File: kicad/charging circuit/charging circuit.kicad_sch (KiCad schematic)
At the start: 21 parts, among them J10 Amphenol PL00Y-301-10M8, J12 Amphenol PL00X-301-10M8, J16 Amphenol PL00X-301-10M8, J17 Amphenol PL00Y-301-10M8, J2 Conn_01x06, J3 Conn_01x08, J34 amphenolpl00Y, J35 Conn_01x03, SW20 SW_Push_Open

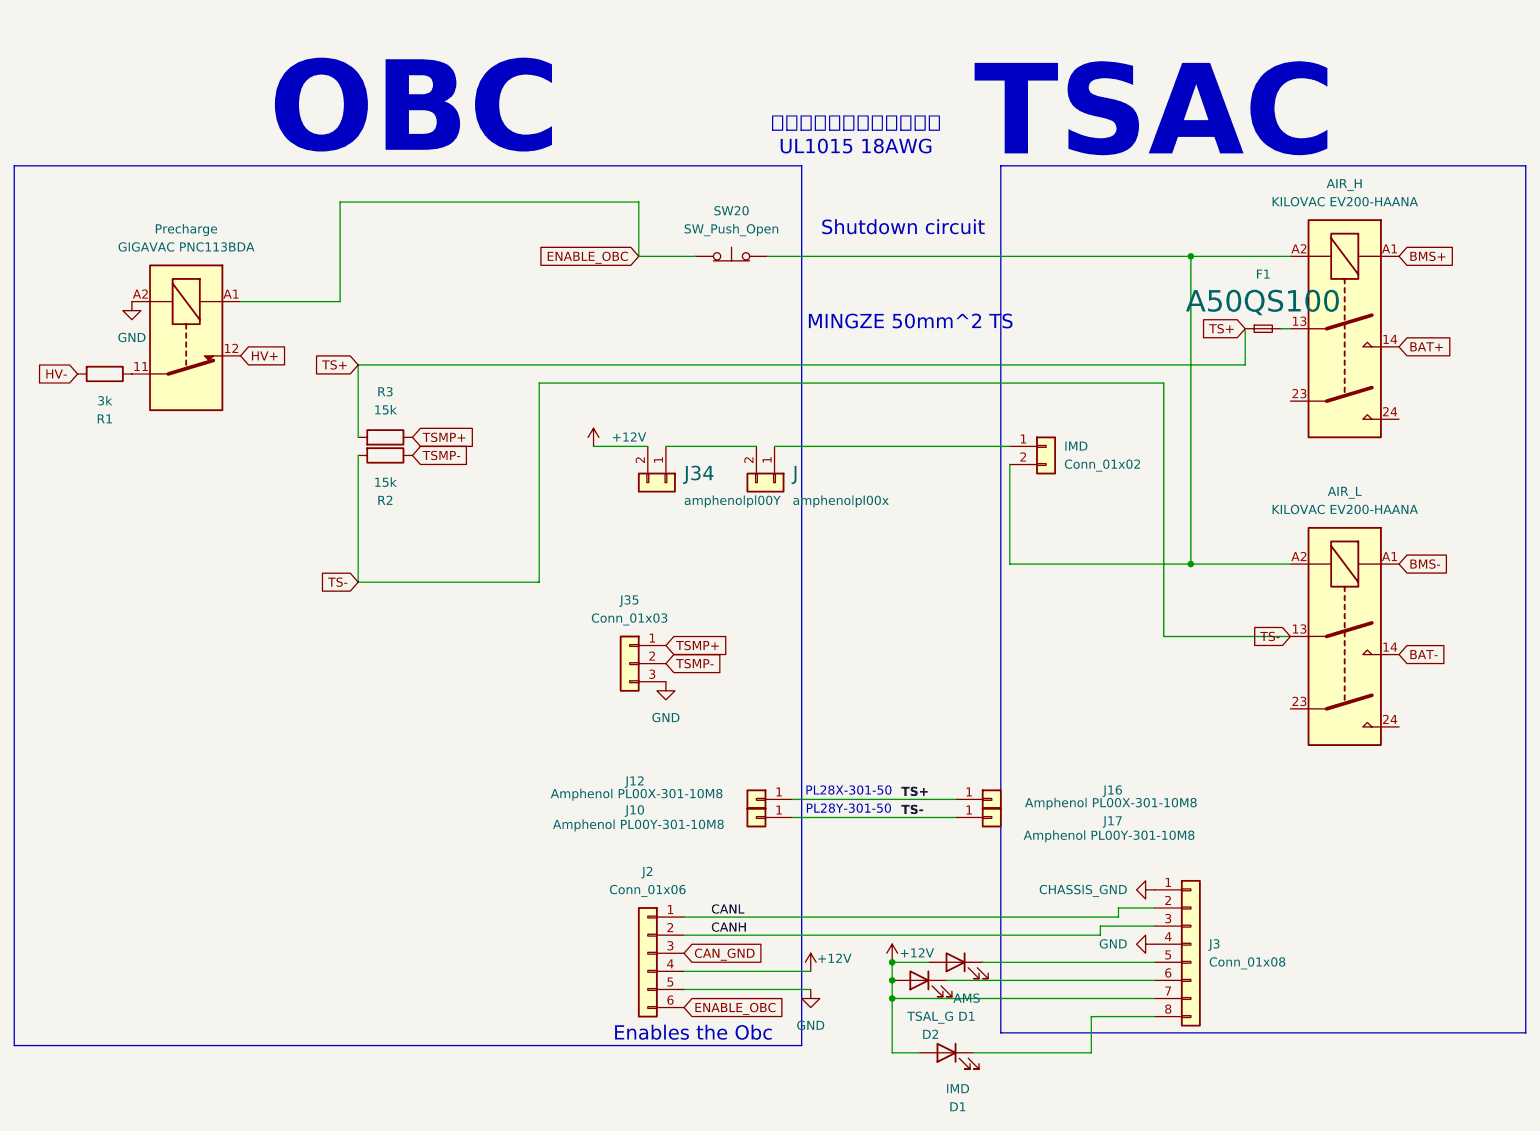
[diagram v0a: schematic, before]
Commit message: what
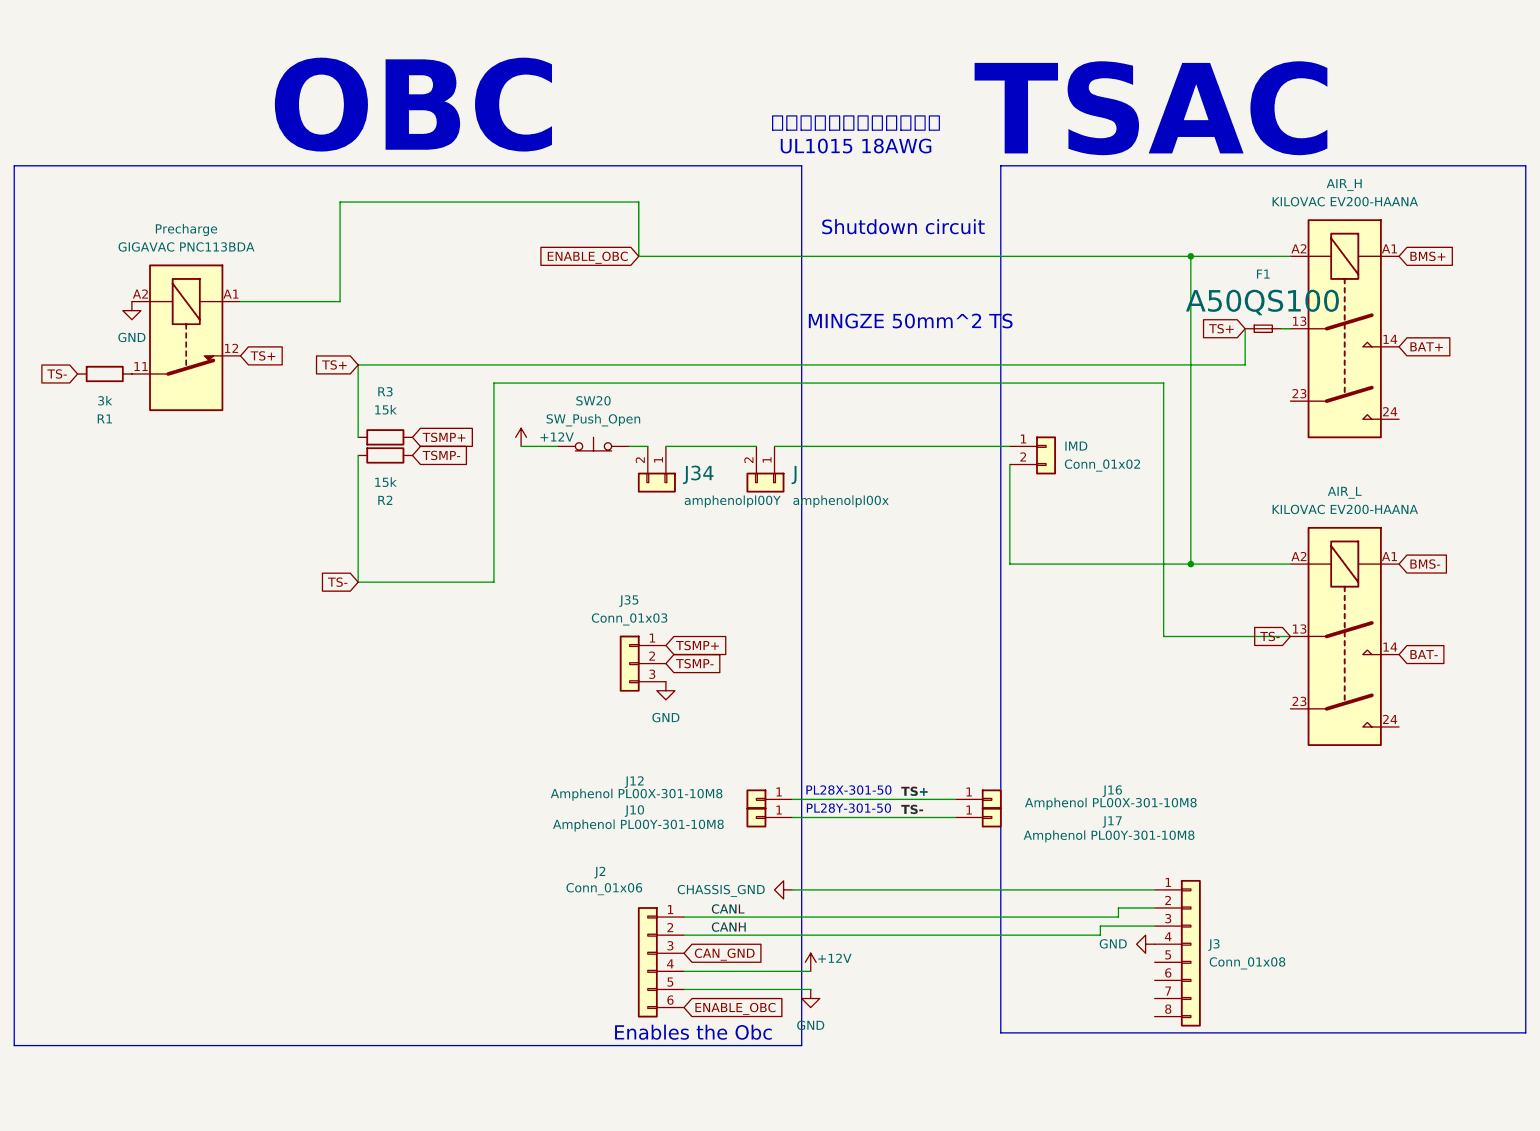
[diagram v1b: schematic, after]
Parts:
- removed D1: AMS, symbol Device:LED
- removed D1: IMD, symbol Device:LED
- removed D2: TSAL_G, symbol Device:LED
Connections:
- net HV+ is gone; now on net TS+: Precharge.12
- net HV- is gone; now on net TS-: R1.2
- net +12V: now also SW20.1 (A); no longer J3.7 (Pin_7), J34.2 (Pin_2)
- net ENABLE_OBC: now also AIR_H.A2, AIR_L.A2, IMD.2 (Pin_2); no longer SW20.1 (A)
- new net: J34.2 (Pin_2), SW20.2 (B)
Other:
- moved on the sheet: SW20
